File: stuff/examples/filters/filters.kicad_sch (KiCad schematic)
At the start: 3 parts, among them U1 MAX7375AXR805

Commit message: Transistor filter (uncompleted)
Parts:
- added Q1: 2N2219, Package_TO_SOT_THT:TO-39-3, symbol Transistor_BJT:2N2219
- added R1: 100R, KIM-1_Library:R_Axial_DIN0309_100R_L6.3mm_D2.5mm_P12.70mm_Horizontal, symbol Device:R_Small
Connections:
- net at R6.1: now also Q1.2 (B); no longer D1.2 (A)
- new net: Q1.3 (C), R1.2
- new net: D1.2 (A), Q1.1 (E)
- new net +5V: R1.1
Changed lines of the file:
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@@
 (kicad_sch (version 20230121) (generator eeschema)
   (paper "A2")
-  (wire (pts (xy 334.01 67.31) (xy 334.01 62.23))
-    (stroke (width 0) (type default))
-  )
-  (wire (pts (xy 334.01 62.23) (xy 317.5 62.23))
+  (wire (pts (xy 326.39 62.23) (xy 317.5 62.23))
     (stroke (width 0) (type default))
   )
@@
         (path "/12882ae0-ee92-4cfd-99ea-b49ca74b2a9a"
           (reference "R6") (unit 1)
+        )
+      )
+    )
+  )
+  (symbol (lib_id "Device:R_Small") (at 334.01 54.61 0) (mirror y) (unit 1)
+    (in_bom yes) (on_board yes) (dnp no)
+    (property "Reference" "R1" (at 328.93 55.88 0)
+      (effects (font (size 1.27 1.27)) (justify right) hide)
+    )
+    (property "Value" "100R" (at 327.66 53.34 0)
+      (effects (font (size 1.27 1.27)) (justify right) hide)
+    )
+    (property "Footprint" "KIM-1_Library:R_Axial_DIN0309_100R_L6.3mm_D2.5mm_P12.70mm_Horizontal" (at 334.01 54.61 0)
+      (effects (font (size 1.27 1.27)) hide)
+    )
+    (property "Datasheet" "~" (at 334.01 54.61 0)
+      (effects (font (size 1.27 1.27)) hide)
+    )
+    (pin "1")
+    (pin "2")
+    (instances
+      (project "filters"
+        (path "/12882ae0-ee92-4cfd-99ea-b49ca74b2a9a"
+          (reference "R1") (unit 1)
         )
       )
@@
         )
       )
+    )
+  )
+  (symbol (lib_id "power:+5V") (at 334.01 52.07 0) (unit 1)
+    (in_bom yes) (on_board yes) (dnp no)
+    (property "Reference" "#PWR01" (at 334.01 55.88 0)
+      (effects (font (size 1.27 1.27)) hide)
+    )
+    (property "Value" "+5V" (at 334.01 48.514 0)
+      (effects (font (size 1.27 1.27)))
+    )
+    (property "Footprint" "" (at 334.01 52.07 0)
+      (effects (font (size 1.27 1.27)) hide)
+    )
+    (property "Datasheet" "" (at 334.01 52.07 0)
+      (effects (font (size 1.27 1.27)) hide)
+    )
+    (pin "1")
+    (instances
+      (project "filters"
+        (path "/12882ae0-ee92-4cfd-99ea-b49ca74b2a9a"
+          (reference "#PWR01") (unit 1)
+        )
+      )
+    )
+  )
+  (symbol (lib_id "Transistor_BJT:2N2219") (at 331.47 62.23 0) (unit 1)
+    (in_bom yes) (on_board yes) (dnp no)
+    (property "Reference" "Q1" (at 336.55 60.325 0)
+      (effects (font (size 1.27 1.27)) (justify left))
+    )
+    (property "Value" "2N2219" (at 336.55 62.23 0)
+      (effects (font (size 1.27 1.27)) (justify left))
+    )
+    (property "Footprint" "Package_TO_SOT_THT:TO-39-3" (at 336.55 64.135 0)
+      (effects (font (size 1.27 1.27) italic) (justify left) hide)
+    )
+    (property "Datasheet" "http://www.onsemi.com/pub_link/Collateral/2N2219-D.PDF" (at 331.47 62.23 0)
+      (effects (font (size 1.27 1.27)) (justify left) hide)
+    )
+    (pin "1")
+    (pin "3")
+    (pin "2")
+    (instances
+      (project "filters"
+        (path "/12882ae0-ee92-4cfd-99ea-b49ca74b2a9a"
+          (reference "Q1") (unit 1)
+        )
+      )

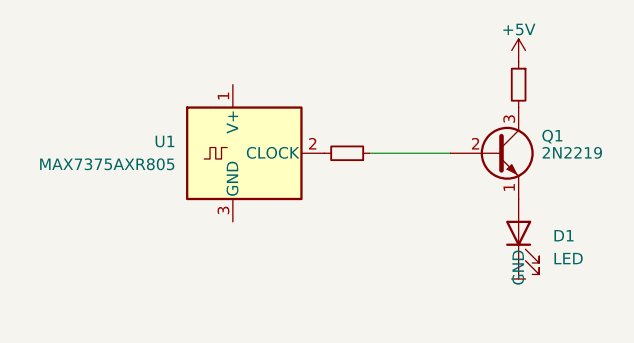
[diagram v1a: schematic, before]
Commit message: Transistor filter fix
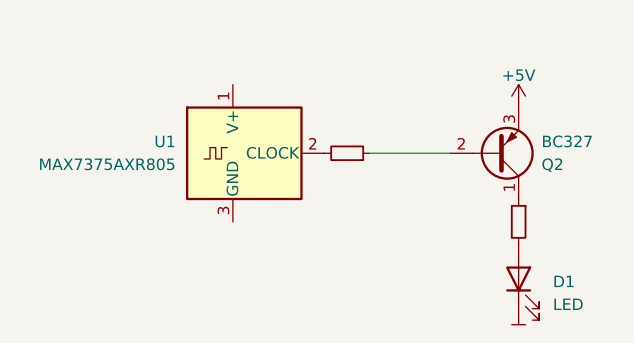
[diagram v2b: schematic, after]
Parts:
- removed Q1: 2N2219, Package_TO_SOT_THT:TO-39-3, symbol Transistor_BJT:2N2219
- added Q2: BC327, Package_TO_SOT_THT:TO-92_Inline, symbol Transistor_BJT:BC327
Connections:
- net +5V: now also Q2.3 (E); no longer R1.1
- net at R6.1: now also Q2.2 (B)
- net at R1.2: now also D1.2 (A)
- net gnd renamed GND
- new net: Q2.1 (C), R1.1
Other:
- moved on the sheet: D1
